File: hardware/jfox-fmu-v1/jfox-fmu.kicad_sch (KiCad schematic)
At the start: 0 parts

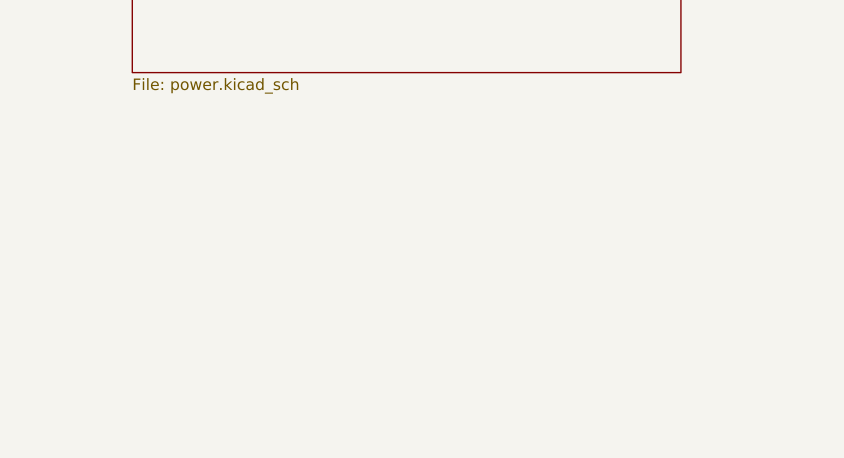
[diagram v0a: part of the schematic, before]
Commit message: Capture the comms sheet: CAN termination behind a jumper, USB-C, microSD
The last sheet, and the one that designs out the defect this whole project
kept working around. Every PX4FMUv2.4.5 carries R409, 120 ohm hard across
CAN_H/CAN_L with no way to remove it short of a soldering iron, so a
three-board bus needs the middle module desoldered - a fact recorded in
HARDWARE_BRINGUP.md, on the carrier silkscreen, and asserted by the TMR
netlist checker. Here each bus gets 120 ohm in series with a solder jumper,
fitted by default. The middle module clears a jumper.

Both CAN buses get a TCAN332 transceiver. v2.4.5 wired CAN2 to the MCU with
no transceiver at all, so it was never usable as a bus.

Also USB-C rather than micro-B, and the microSD on SDMMC1's full 4-bit
interface - which is why the third IMU sits on SPI6: SPI3's only pins on this
part are PC10/11/12, which are also SDMMC1's CK/D2/D3, and the allocator
found that rather than anyone guessing.

check_fmu_schematic gains the capstone assertion: sixteen nets must span
sheets and join named parts - MCU to both CAN transceivers, to USB-C, to the
microSD, to each IMU, to the FRAM, to the barometer, and to each load switch.
That proves the four sheets are one circuit rather than four drawings that
happen to use similar label names. It matters because global labels only
connect once the sheets share a root, and before that root existed every one
of these read as isolated at both ends.

Six checks now, all passing, all negative-tested.

ERC across the assembled project reports 176 violations, all explainable:
unallocated MCU GPIO left free for a later revision, UART and PWM nets whose
connectors are not drawn yet, and rails with no PWR_FLAG. None are wiring
faults - the interconnect is verified by the checks above.

Co-Authored-By: Claude Opus 5 <noreply@anthropic.com>
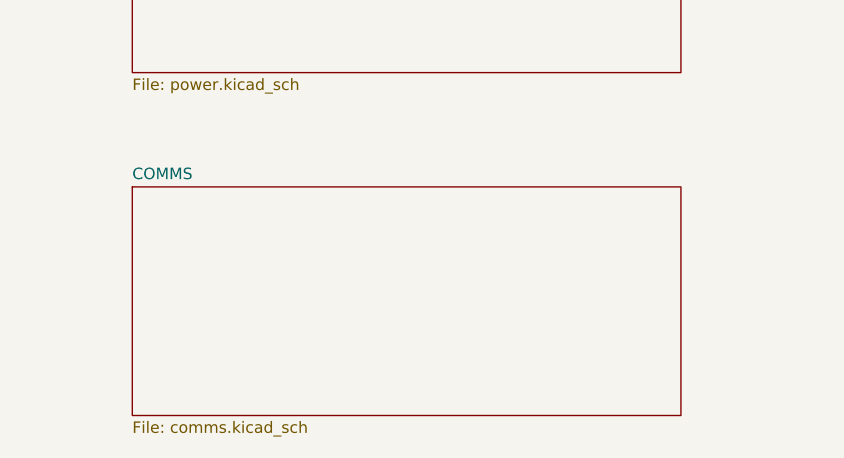
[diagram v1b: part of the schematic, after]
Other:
- added sheet COMMS (comms.kicad_sch)
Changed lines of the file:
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@@
 		(instances
 			(project "jfox-fmu"
-				(path "/650f07a7-2d18-4de2-ac87-cdeec4948d34"
+				(path "/2ddf097b-38c1-41be-a06d-3f4921faa6d2"
 					(page "2")
 				)
@@
 		(instances
 			(project "jfox-fmu"
-				(path "/650f07a7-2d18-4de2-ac87-cdeec4948d34"
+				(path "/2ddf097b-38c1-41be-a06d-3f4921faa6d2"
 					(page "3")
 				)
@@
 		(instances
 			(project "jfox-fmu"
-				(path "/650f07a7-2d18-4de2-ac87-cdeec4948d34"
+				(path "/2ddf097b-38c1-41be-a06d-3f4921faa6d2"
 					(page "4")
 				)
 			)
+		)
+	)
+	(sheet
+		(at 38.1 203.20000000000002)
+		(size 60.96 25.4)
+		(fields_autoplaced yes)
+		(stroke (width 0.1524)(type solid))
+		(fill (color 0 0 0 0.0000))
+		(property "Sheetname" "COMMS"
+			(at 38.1 202.49 0)
+			(effects (font (size 1.27 1.27))(justify left bottom))
+		)
+		(property "Sheetfile" "comms.kicad_sch"
+			(at 38.1 229.2 0)
+			(effects (font (size 1.27 1.27))(justify left top))
+		)
+		(instances
+			(project "jfox-fmu"
+				(path "/2ddf097b-38c1-41be-a06d-3f4921faa6d2"
+					(page "5")
+				)
+			)

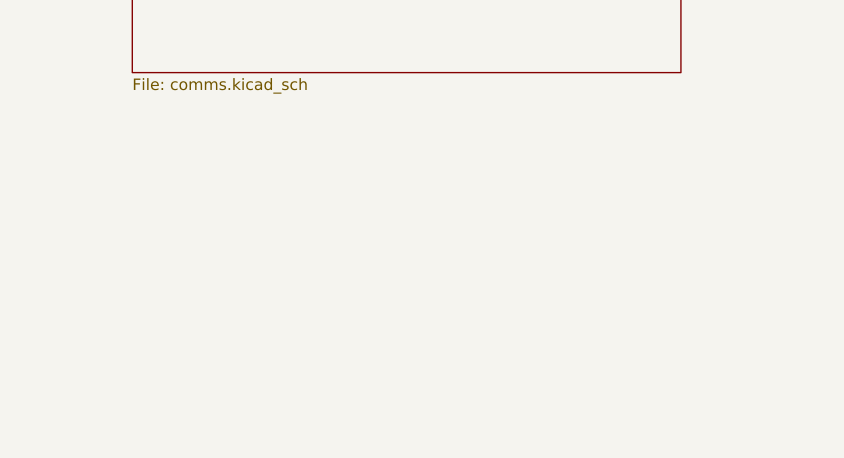
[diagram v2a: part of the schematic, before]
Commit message: Add the passives a board cannot be built without
Decoupling (one 100n per MCU VDD pin plus bulk per rail), the internal LDO's
two 2.2 uF VCAP capacitors, both crystals with their load caps, the TPS62130's
inductor and feedback divider, and the two 120R CAN terminators - which until
now existed only as a note on the comms sheet, which is to say not at all.

36 two-pin parts, 2 crystals, 7 PWR_FLAGs. ERC drops 264 to 181.

Two silent-failure bugs in the generator, both found by the counts rather than
by looking:

Passive symbols name both pins the empty string, and the pin-geometry helper
keyed by name, so a name-keyed dict kept one pin and dropped the other. Every
capacitor got one end wired. Added pin_list, which keys by nothing and returns
every pin; pin_positions stays for the MCU, where names are what matter.

The pin regex also required at least one character in the name, so on parts
whose pins are named "" it matched nothing at all and returned zero pins. One
character in a pattern, 84 unconnected pins.

The new check asserts what ERC structurally cannot: a missing decoupling
capacitor fails no rule, blocks no fabrication, and shows up as an MCU that
resets under load. So the capacitor count, the VCAP capacitors, both crystals
and both CAN terminators are asserted by name.

That check was also wrong on its first run, in exactly the way the power check
was wrong before it: comparing bare reference designators, so U10 having both
VCAP pins and VDD pins "proved" VCAP was shorted to +3V3 on a correct
schematic. Fixed to compare (ref, pin), and the reason is now written at the
comparison so it stops recurring.

Seven checks, all passing, all negative-tested.

Co-Authored-By: Claude Opus 5 <noreply@anthropic.com>
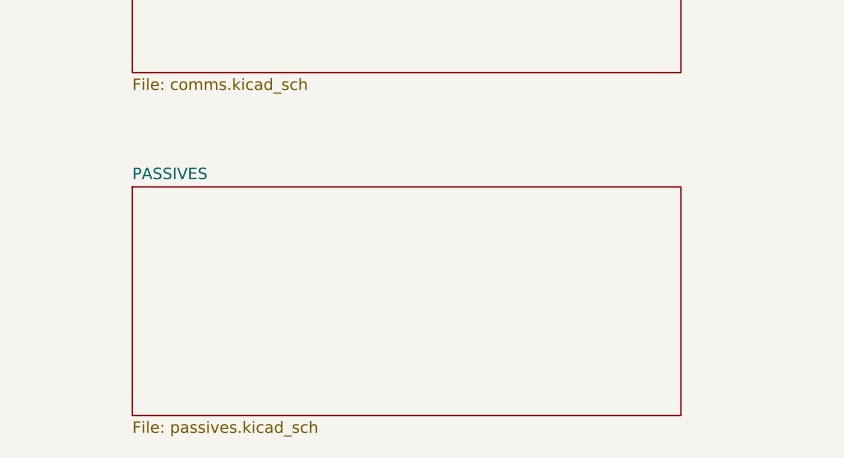
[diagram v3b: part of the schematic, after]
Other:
- added sheet PASSIVES (passives.kicad_sch)
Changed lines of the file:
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@@
 		(instances
 			(project "jfox-fmu"
-				(path "/091b9e38-8612-4a3b-aa40-ea2c03740cd5"
+				(path "/e3cafe2c-5116-467a-b4ca-5a381e686c9d"
 					(page "2")
 				)
@@
 		(instances
 			(project "jfox-fmu"
-				(path "/091b9e38-8612-4a3b-aa40-ea2c03740cd5"
+				(path "/e3cafe2c-5116-467a-b4ca-5a381e686c9d"
 					(page "3")
 				)
@@
 		(instances
 			(project "jfox-fmu"
-				(path "/091b9e38-8612-4a3b-aa40-ea2c03740cd5"
+				(path "/e3cafe2c-5116-467a-b4ca-5a381e686c9d"
 					(page "4")
 				)
@@
 		(instances
 			(project "jfox-fmu"
-				(path "/091b9e38-8612-4a3b-aa40-ea2c03740cd5"
+				(path "/e3cafe2c-5116-467a-b4ca-5a381e686c9d"
 					(page "5")
 				)
 			)
+		)
+	)
+	(sheet
+		(at 38.1 241.3)
+		(size 60.96 25.4)
+		(fields_autoplaced yes)
+		(stroke (width 0.1524)(type solid))
+		(fill (color 0 0 0 0.0000))
+		(property "Sheetname" "PASSIVES"
+			(at 38.1 240.59 0)
+			(effects (font (size 1.27 1.27))(justify left bottom))
+		)
+		(property "Sheetfile" "passives.kicad_sch"
+			(at 38.1 267.3 0)
+			(effects (font (size 1.27 1.27))(justify left top))
+		)
+		(instances
+			(project "jfox-fmu"
+				(path "/e3cafe2c-5116-467a-b4ca-5a381e686c9d"
+					(page "6")
+				)
+			)

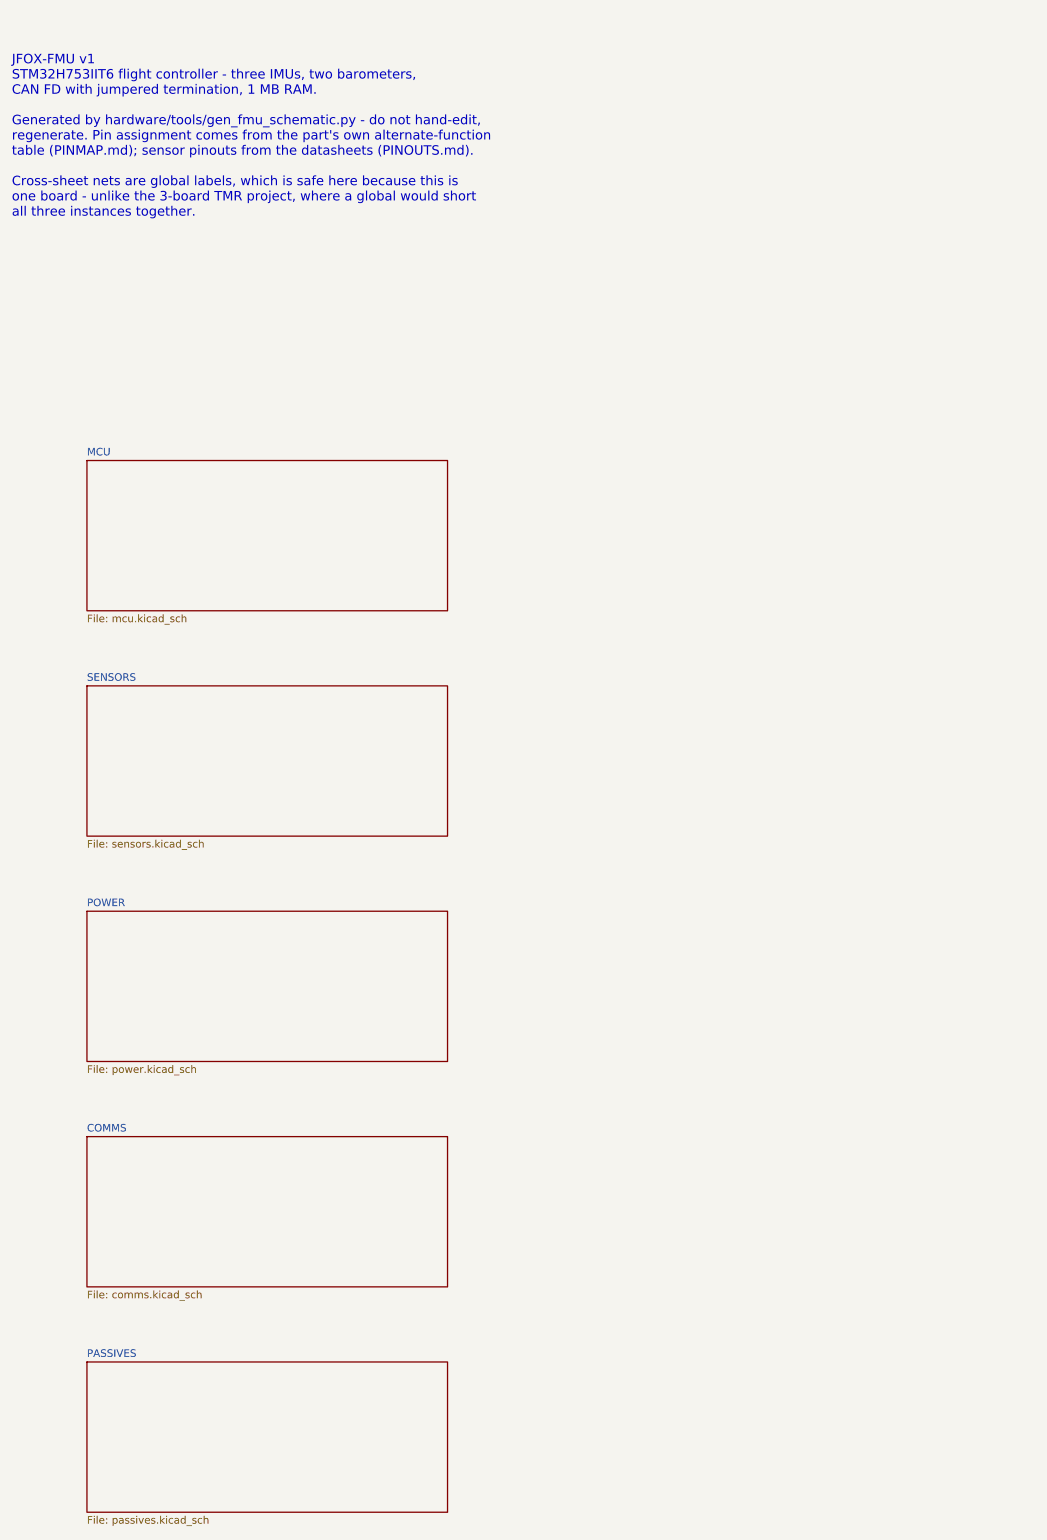
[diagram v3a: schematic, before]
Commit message: A4 title-blocked sheets, and the 25 power pins that were never wired
Every sheet now carries a title block naming JFOX Aircraft Co., Ltd., with a
per-sheet title, revision, date and the notes that used to float as loose text.

A4 PORTRAIT, not landscape, and not by preference. The STM32H753IITx symbol is
a single unit - KiCad's library gives it only _0_1 body and _1_1 pin
sub-symbols, so it cannot be split across pages - and its 176 pins span
231.1 mm. A4 landscape offers about 180 mm of usable height and would cut the
MCU in half. Portrait offers 237 mm. The part fits with 2 mm to spare, which
is why the page margin is 2 mm: it is the largest margin that still holds an
LQFP176, not a number chosen for looks.

The frame geometry was measured, not assumed - an empty A4 portrait sheet
plotted through kicad-cli, frame read off the SVG at 12,12 -> 198,285 with the
title block claiming x >= 90, y >= 253.

Three defects the work surfaced, in rising order of how much they mattered:

Every sheet had content at negative coordinates, off the page entirely, where
KiCad edits it happily and the plotter crops it away. Nothing had complained
because nothing was looking. fit() now translates each sheet into the drawable
area and refuses - loudly - to emit one that does not fit, because a schematic
that is silently cropped lies about the board.

fit() then passed the power sheet while its rightmost label sat 8.6 mm past
the frame. A global label's angle is the direction its CONNECTION faces, so
the text runs the opposite way; reading it the intuitive way put every
estimated extent on the wrong side of its anchor. That is worse than not
estimating: it reports "inside the frame" precisely when labels hang off it.
Caught by measuring KiCad's own plotted geometry instead of trusting the
estimate - which is what check_fmu_sheets.py now does on every sheet, with
--exclude-drawing-sheet so only the circuit is measured.

And centring the sheets by (SAFE_W - w) / 2 shifted every wire off th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
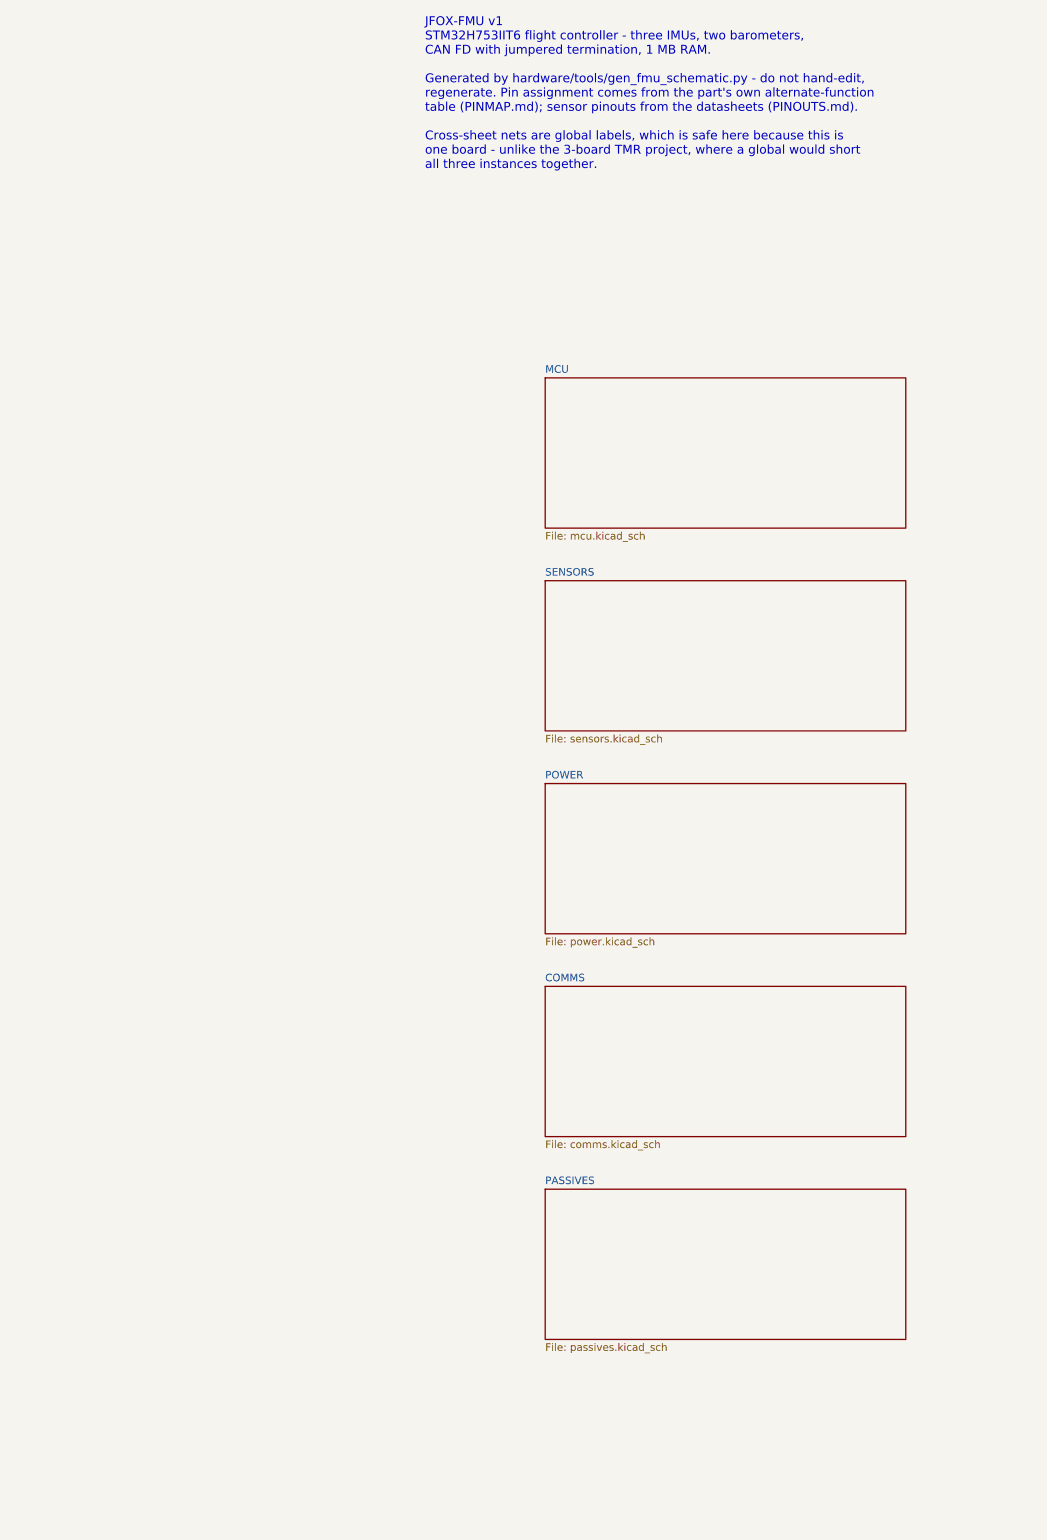
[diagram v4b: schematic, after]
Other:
- company: (none) -> JFOX Aircraft Co., Ltd.
- title: (none) -> JFOX-FMU v1
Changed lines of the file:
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@@
 	(generator "jfox gen_fmu_schematic")
 	(generator_version "10.0")
-	(paper "A3")
+	(paper "A4" portrait)
+	(title_block
+		(title "JFOX-FMU v1")
+		(date "2026-08-03")
+		(rev "A")
+		(company "JFOX Aircraft Co., Ltd.")
+		(comment 1 "STM32H753IIT6 - 3 IMUs, 2 barometers, magnetometer, CAN FD")
+		(comment 2 "Generated by hardware/tools/gen_fmu_schematic.py - regenerate, do not edit")
+		(comment 3 "Sheet 1 of 6")
+	)
 	(text "JFOX-FMU v1\nSTM32H753IIT6 flight controller - three IMUs, two barometers,\nCAN FD with jumpered termination, 1 MB RAM.\n\nGenerated by hardware/tools/gen_fmu_schematic.py - do not hand-edit,\nregenerate. Pin assignment comes from the part's own alternate-function\ntable (PINMAP.md); sensor pinouts from the datasheets (PINOUTS.md).\n\nCross-sheet nets are global labels, which is safe here because this is\none board - unlike the 3-board TMR project, where a global would short\nall three instances together."
-		(at 25.4 20.32 0)
+		(at 95.25 13.97 0)
 		(effects
 			(font
-				(size 1.6 1.6)
+				(size 1.5 1.5)
 			)
 			(justify left top)
@@
 	)
 	(sheet
-		(at 38.1 88.9)
+		(at 115.57 74.93)
 		(size 60.96 25.4)
 		(fields_autoplaced yes)
@@
 		(fill (color 0 0 0 0.0000))
 		(property "Sheetname" "MCU"
-			(at 38.1 88.19 0)
+			(at 115.57 74.22 0)
 			(effects (font (size 1.27 1.27))(justify left bottom))
 		)
 		(property "Sheetfile" "mcu.kicad_sch"
-			(at 38.1 114.9 0)
+			(at 115.57 100.93 0)
 			(effects (font (size 1.27 1.27))(justify left top))
 		)
 		(instances
 			(project "jfox-fmu"
-				(path "/e3cafe2c-5116-467a-b4ca-5a381e686c9d"
+				(path "/f745e5d3-d017-45e5-b315-b341675755b4"
 					(page "2")
 				)
@@
 	)
 	(sheet
-		(at 38.1 127.0)
+		(at 115.57 109.22)
 		(size 60.96 25.4)
 		(fields_autoplaced yes)
@@
 		(fill (color 0 0 0 0.0000))
 		(property "Sheetname" "SENSORS"
-			(at 38.1 126.29 0)
+			(at 115.57 108.51 0)
 			(effects (font (size 1.27 1.27))(justify left bottom))
 		)
 		(property "Sheetfile" "sensors.kicad_sch"
-			(at 38.1 153.0 0)
+			(at 115.57 135.22 0)
 			(effects (font (size 1.27 1.27))(justify left top))
 		)
 		(instances
 			(project "jfox-fmu"
-				(path "/e3cafe2c-5116-467a-b4ca-5a381e686c9d"
+				(path "/f745e5d3-d017-45e5-b315-b341675755b4"
 					(page "3")
 				)
@@
 	)
 	(sheet
-		(at 38.1 165.10000000000002)
+		(at 115.57 143.51)
 		(size 60.96 25.4)
 		(fields_autoplaced yes)
@@
 		(fill (color 0 0 0 0.0000))
 		(property "Sheetname" "POWER"
-			(at 38.1 164.39 0)
+			(at 115.57 142.8 0)
 			(effects (font (size 1.27 1.27))(justify left bottom))
 		)
 		(property "Sheetfile" "power.kicad_sch"
-			(at 38.1 191.1 0)
+			(at 115.57 169.51 0)
 			(effects (font (size 1.27 1.27))(justify left top))
 		)
 		(instances
 			(project "jfox-fmu"
-				(path "/e3cafe2c-5116-467a-b4ca-5a381e686c9d"
+				(path "/f745e5d3-d017-45e5-b315-b341675755b4"
 					(page "4")
 				)
@@
 	)
 	(sheet
-		(at 38.1 203.20000000000002)
+		(at 115.57 177.8)
 		(size 60.96 25.4)
 		(fields_autoplaced yes)
@@
 		(fill (color 0 0 0 0.0000))
 		(property "Sheetname" "COMMS"
-			(at 38.1 202.49 0)
+			(at 115.57 177.09 0)
 			(effects (font (size 1.27 1.27))(justify left bottom))
 		)
 		(property "Sheetfile" "comms.kicad_sch"
-			(at 38.1 229.2 0)
+			(at 115.57 203.8 0)
 			(effects (font (size 1.27 1.27))(justify left top))
 		)
 		(instances
 			(project "jfox-fmu"
-				(path "/e3cafe2c-5116-467a-b4ca-5a381e686c9d"
+				(path "/f745e5d3-d017-45e5-b315-b341675755b4"
 					(page "5")
 				)
@@
 	)
 	(sheet
-		(at 38.1 241.3)
+		(at 115.57 212.09)
 		(size 60.96 25.4)
 		(fields_autoplaced yes)
@@
 		(fill (color 0 0 0 0.0000))
 		(property "Sheetname" "PASSIVES"
-			(at 38.1 240.59 0)
+			(at 115.57 211.38 0)
 			(effects (font (size 1.27 1.27))(justify left bottom))
 		)
 		(property "Sheetfile" "passives.kicad_sch"
-			(at 38.1 267.3 0)
+			(at 115.57 238.09 0)
 			(effects (font (size 1.27 1.27))(justify left top))
 		)
 		(instances
 			(project "jfox-fmu"
-				(path "/e3cafe2c-5116-467a-b4ca-5a381e686c9d"
+				(path "/f745e5d3-d017-45e5-b315-b341675755b4"
 					(page "6")
 				)
